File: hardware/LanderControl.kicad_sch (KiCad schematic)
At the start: 25 parts, among them J5 MEM2051-00-195-00-A, U1 SC0915

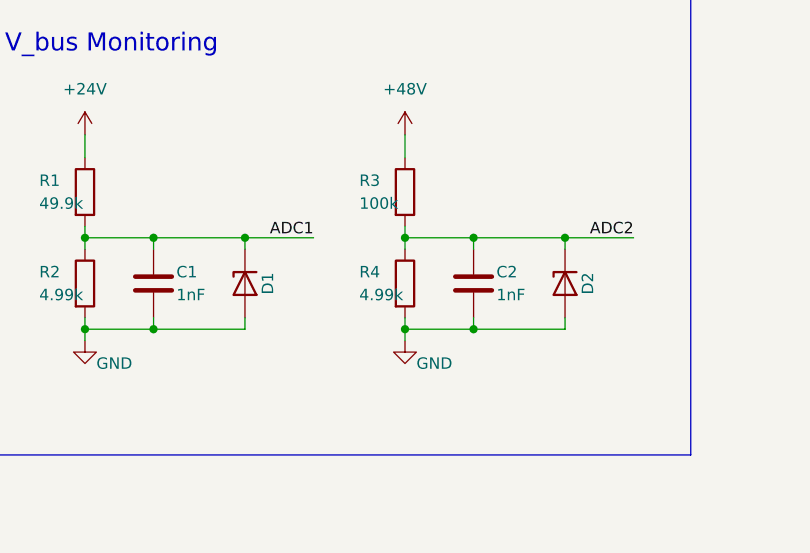
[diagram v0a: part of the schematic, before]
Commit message: Remove diodes from voltage monitoring circuit
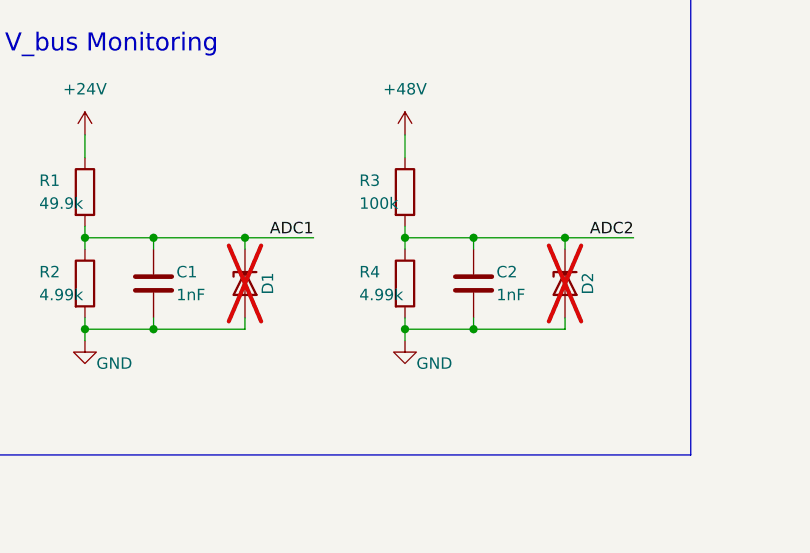
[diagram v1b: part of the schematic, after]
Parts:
- D1, D2: now not fitted; now left out of the parts list
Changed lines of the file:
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@@
   )
   (symbol (lib_id "Device:D_Zener") (at 64.77 231.14 90) (mirror x) (unit 1)
-    (in_bom yes) (on_board yes) (dnp no)
+    (in_bom no) (on_board yes) (dnp yes)
     (property "Reference" "D1" (at 67.31 231.14 0)
       (effects (font (size 1.27 1.27)))
@@
   )
   (symbol (lib_id "Device:D_Zener") (at 100.33 231.14 90) (mirror x) (unit 1)
-    (in_bom yes) (on_board yes) (dnp no)
+    (in_bom no) (on_board yes) (dnp yes)
     (property "Reference" "D2" (at 102.87 231.14 0)
       (effects (font (size 1.27 1.27)))
